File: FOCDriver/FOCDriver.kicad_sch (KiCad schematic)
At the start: 7 parts, among them J6 Conn_01x03_Pin, J7 Conn_01x03_Pin, J8 Conn_01x03_Pin

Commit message: Update
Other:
- sheet MCU ports: added none; removed TIM2_CH1, TIM2_CH2, TIM4_CH1, TIM4_CH2, TIM4_CH3, TIM4_CH4
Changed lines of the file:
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@@
-			)
-		)
-		(pin "TIM2_CH2" input
-			(at 74.93 57.15 0)
-			(effects
-				(font
-					(size 1.27 1.27)
-				)
-				(justify right)
 			)
 		)
@@
 		(pin "ADC1_INP3" input
 			(at 74.93 120.65 0)
-			(effects
-				(font
-					(size 1.27 1.27)
-				)
-				(justify right)
-			)
-		)
-		(pin "TIM4_CH1" input
-			(at 74.93 80.01 0)
-			(effects
-				(font
-					(size 1.27 1.27)
-				)
-				(justify right)
-			)
-		)
-		(pin "TIM4_CH2" input
-			(at 74.93 82.55 0)
-			(effects
-				(font
-					(size 1.27 1.27)
-				)
-				(justify right)
-			)
-		)
-		(pin "TIM4_CH3" input
-			(at 74.93 85.09 0)
-			(effects
-				(font
-					(size 1.27 1.27)
-				)
-				(justify right)
-			)
-		)
-		(pin "TIM4_CH4" input
-			(at 74.93 87.63 0)
 			(effects
 				(font
@@
 			(effects
 				(font
-					(size 1.27 1.27)
-				)
-				(justify right)
-			)
-		)
-		(pin "TIM2_CH1" input
-			(at 74.93 54.61 0)
-			(effects
-				(font

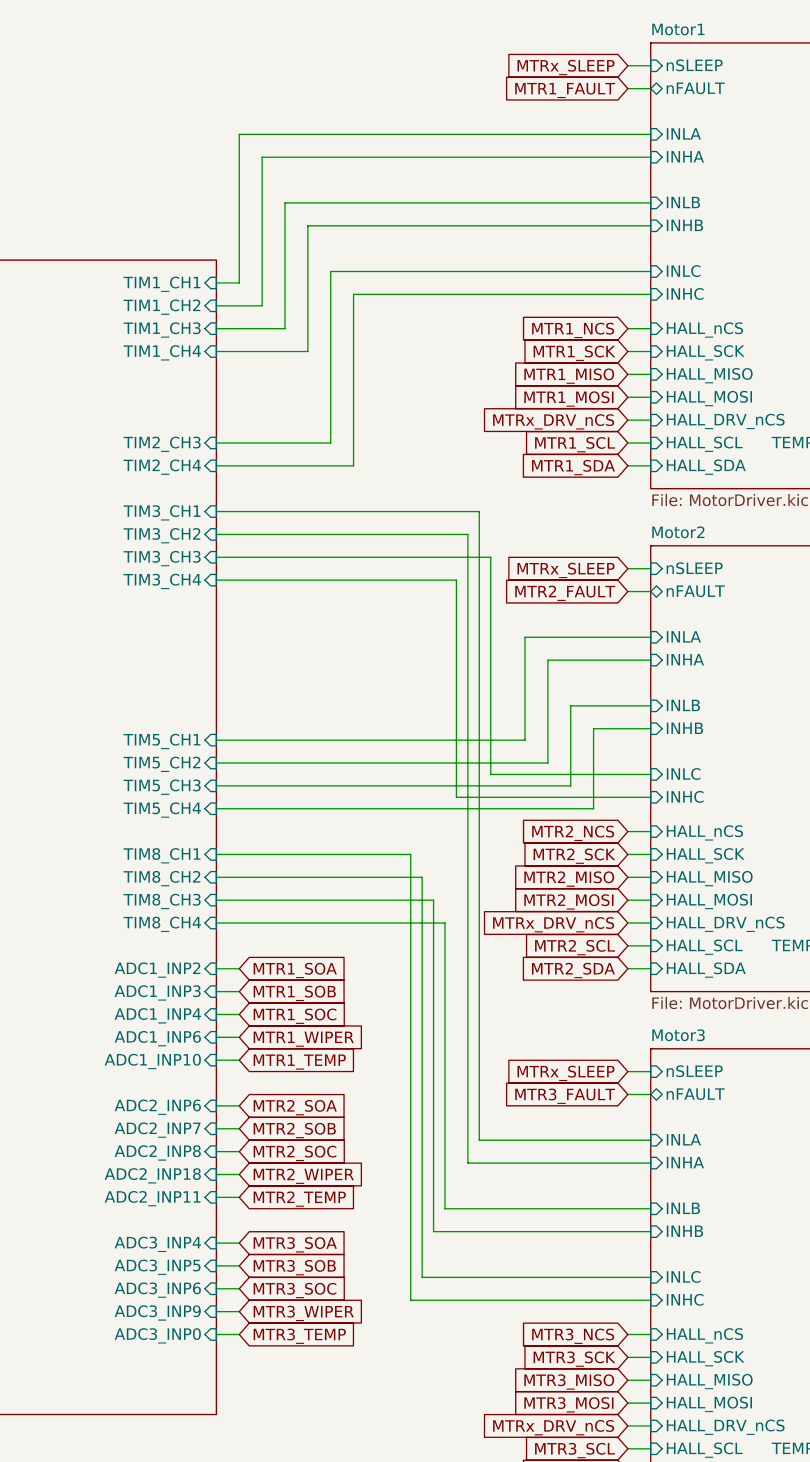
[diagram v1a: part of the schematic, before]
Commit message: Sensor PCB fixes labels
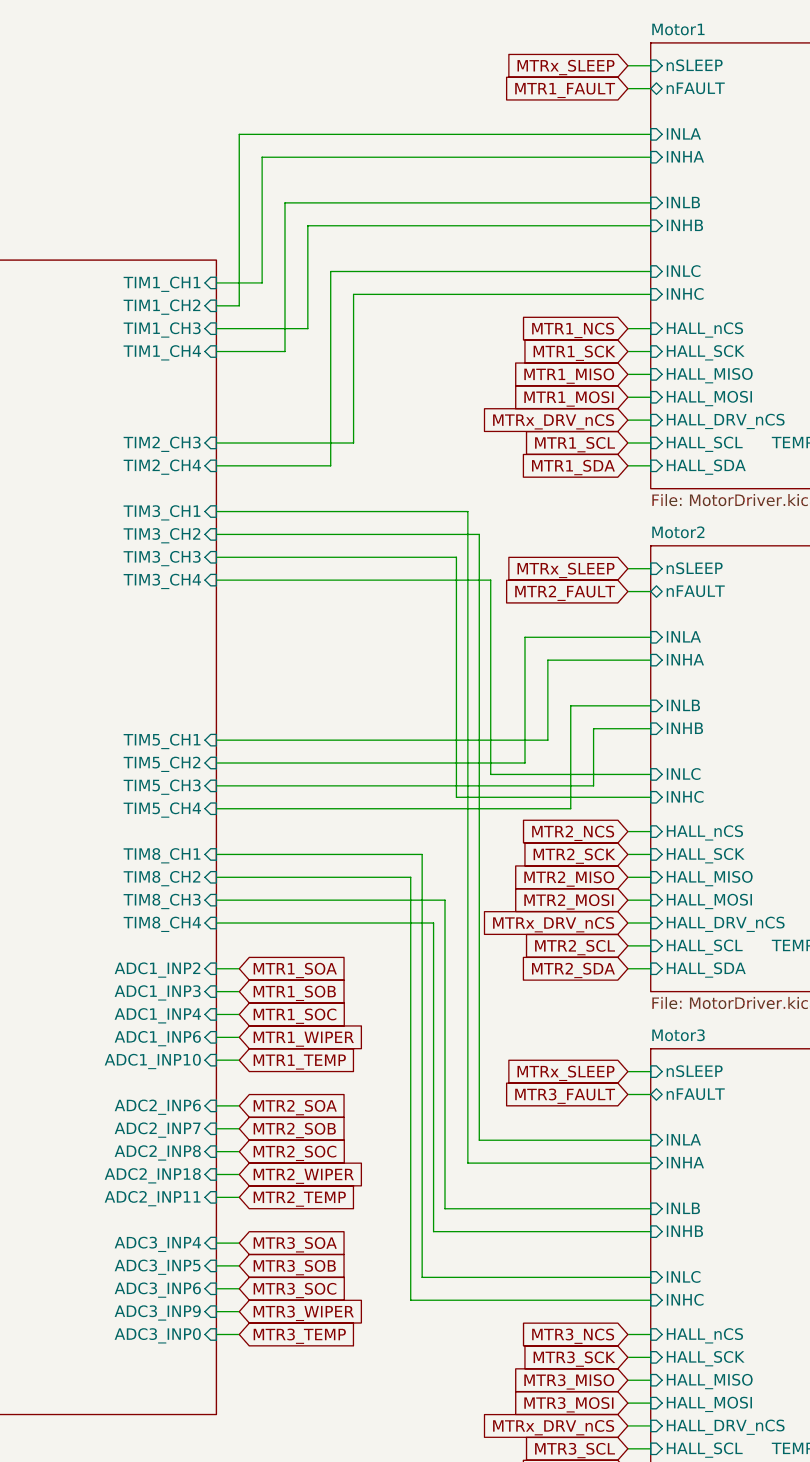
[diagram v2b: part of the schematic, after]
